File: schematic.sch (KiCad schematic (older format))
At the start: 30 parts

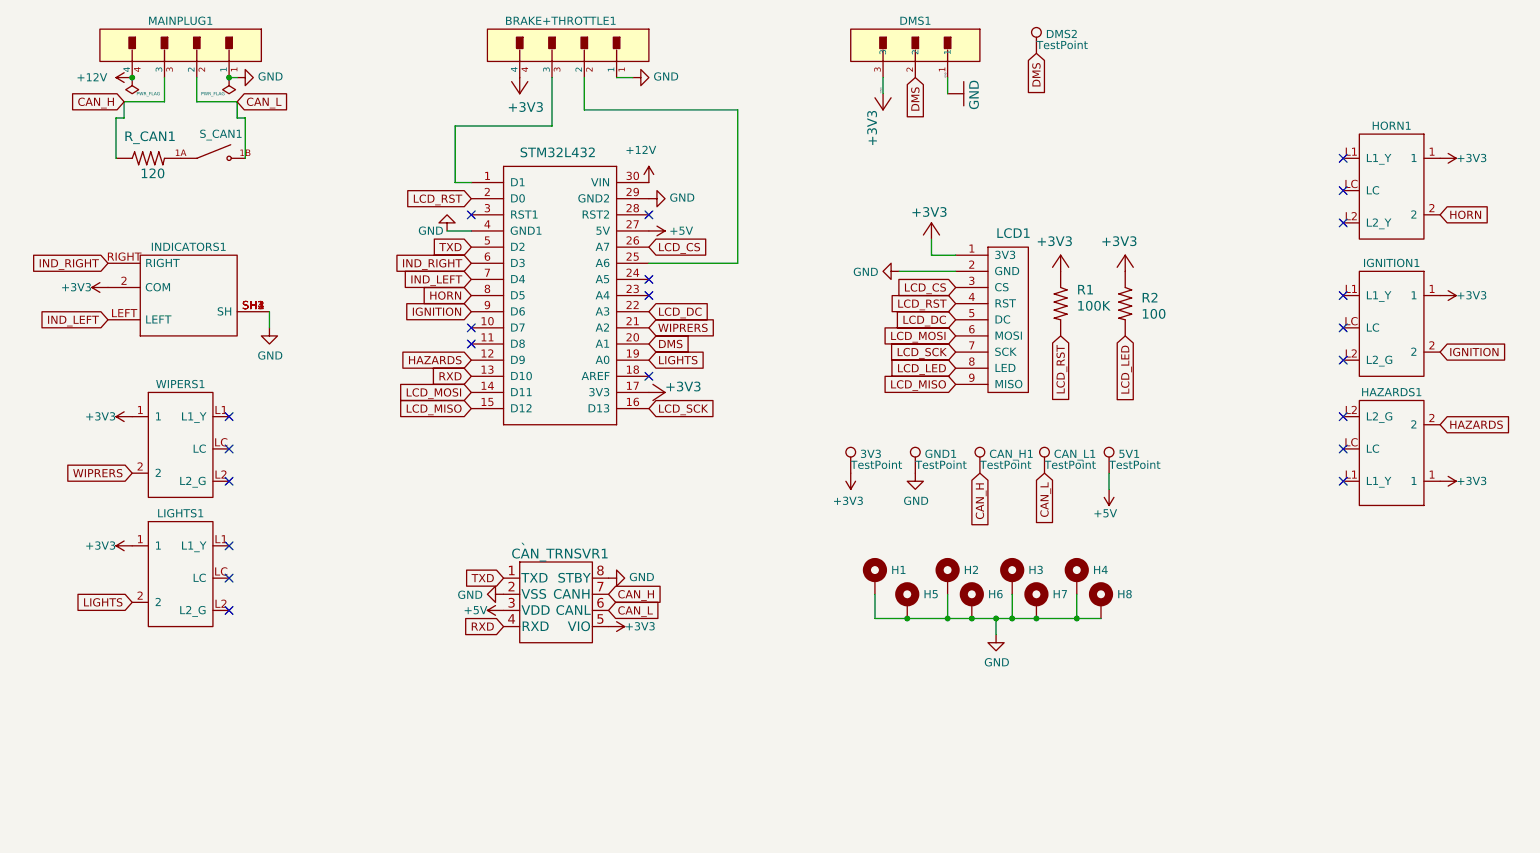
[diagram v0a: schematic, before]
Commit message: Cleaned up project structure, schematic and mask. Changed the DC connection for the TFT
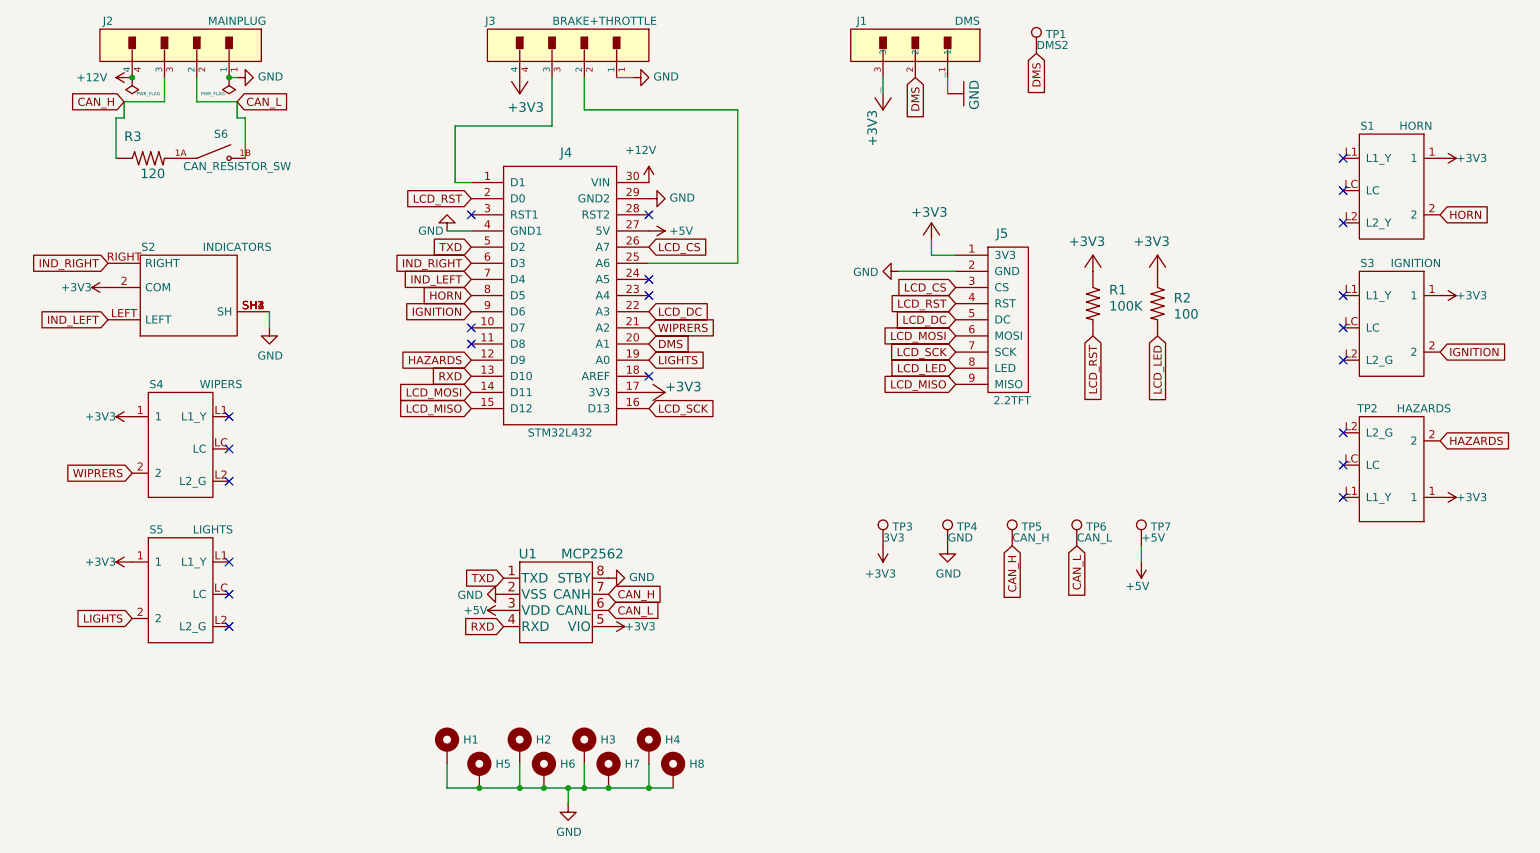
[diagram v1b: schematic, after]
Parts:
- J1: renamed from DMS1; value ` -> DMS
- J2: renamed from MAINPLUG1; value MOLEX-15-91-2045-PIN_HEADER -> MAINPLUG
- J3: renamed from BRAKE+THROTTLE1; value ` -> BRAKE+THROTTLE
- S1: renamed from HORN1; value ` -> HORN
- S2: renamed from INDICATORS1; value ` -> INDICATORS; footprint M2013TXG13DA -> M2013TXG13DA:M2013TXG13DA
- S3: renamed from IGNITION1; value ` -> IGNITION
- S4: renamed from WIPERS1; value ` -> WIPERS
- S5: renamed from LIGHTS1; value ` -> LIGHTS
- S6: renamed from S_CAN1; value ~ -> CAN_RESISTOR_SW; footprint SW_DS04-254-2-01BK-SMT -> dip_swtich_1pos:SW_DS04-254-2-01BK-SMT
- TP1: renamed from DMS2; value TestPoint -> DMS2
- TP2: renamed from HAZARDS1; value ` -> HAZARDS
- TP3: renamed from 3V3; value TestPoint -> 3V3
- TP4: renamed from GND1; value TestPoint -> GND
- TP5: renamed from CAN_H1; value TestPoint -> CAN_H
- TP6: renamed from CAN_L1; value TestPoint -> CAN_L
- TP7: renamed from 5V1; value TestPoint -> +5V
- U1: renamed from CAN_TRNSVR1; value ` -> MCP2562
- renumbered STM32L432 to J4, LCD1 to J5, R_CAN1 to R3
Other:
- moved on the sheet: H1, H2, H3, H4, H5, H6, H7, H8, R1, R2, S5, TP2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
